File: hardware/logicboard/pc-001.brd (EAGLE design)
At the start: 25 x 61.5 mm, 15 parts, among them J4 DNP, J5 DNP

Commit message: OSHW logo.
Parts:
- added LOGO1: OSHW-LOGOL, SparkFun-Aesthetics:OSHW-LOGO-L
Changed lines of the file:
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@@
 <layer number="26" name="bNames" color="7" fill="1" visible="yes" active="yes"/>
 <layer number="27" name="tValues" color="7" fill="1" visible="yes" active="yes"/>
-<layer number="28" name="bValues" color="7" fill="1" visible="yes" active="yes"/>
+<layer number="28" name="bValues" color="7" fill="1" visible="no" active="yes"/>
 <layer number="29" name="tStop" color="7" fill="3" visible="yes" active="yes"/>
 <layer number="30" name="bStop" color="7" fill="6" visible="yes" active="yes"/>
@@
 <element name="J5" library="SparkFun-Connectors" library_urn="urn:adsk.eagle:library:513" package="1X14" package3d_urn="urn:adsk.eagle:package:38183/1" value="DNP" x="22.66" y="6.3516" smashed="yes" rot="R90">
 <attribute name="NAME" x="22.66" y="42" size="0.6096" layer="25" font="vector" ratio="20" rot="R90" align="center"/>
-<attribute name="VALUE" x="24.692" y="5.0816" size="0.6096" layer="27" font="vector" ratio="20" rot="R90"/>
+<attribute name="VALUE" x="24.692" y="5.0816" size="0.6096" layer="26" font="vector" ratio="20" rot="R90"/>
 </element>
 <element name="J4" library="SparkFun-Connectors" library_urn="urn:adsk.eagle:library:513" package="1X14" package3d_urn="urn:adsk.eagle:package:38183/1" value="DNP" x="2.34" y="39.3716" smashed="yes" rot="R270">
 <attribute name="NAME" x="2.34" y="42" size="0.6096" layer="25" font="vector" ratio="20" rot="R270" align="center"/>
-<attribute name="VALUE" x="0.308" y="40.6416" size="0.6096" layer="27" font="vector" ratio="20" rot="R270"/>
+<attribute name="VALUE" x="0.308" y="40.6416" size="0.6096" layer="26" font="vector" ratio="20" rot="R270"/>
 </element>
 <element name="RN1" library="resistor-net" library_urn="urn:adsk.eagle:library:343" package="RN-5" package3d_urn="urn:adsk.eagle:package:24976/1" value="10k" x="5.5" y="37" smashed="yes" rot="MR270">
@@
 <attribute name="VALUE" x="20.12" y="12.268" size="0.6096" layer="28" font="vector" ratio="20" rot="MR0"/>
 </element>
+<element name="LOGO1" library="SparkFun-Aesthetics" package="OSHW-LOGO-L" value="OSHW-LOGOL" x="12.5" y="53"/>
 </elements>
 <signals>

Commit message: Pineapple logo v2.
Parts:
- added U$1: PINEAPPLELOGO2, pineapplelogo2:PINEAPPLELOGO2
- LOGO1: value OSHW-LOGOL -> OSHW-LOGOS-COPPER; device SparkFun-Aesthetics:OSHW-LOGO-L -> SparkFun-Aesthetics:OSHW-LOGO-S_COPPER
- moved LOGO1 1.00 mm to (12.5, 52.0)
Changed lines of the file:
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@@
 <layers>
 <layer number="1" name="Top" color="4" fill="1" visible="yes" active="yes"/>
-<layer number="16" name="Bottom" color="1" fill="1" visible="yes" active="yes"/>
+<layer number="16" name="Bottom" color="1" fill="1" visible="no" active="yes"/>
 <layer number="17" name="Pads" color="2" fill="1" visible="yes" active="yes"/>
 <layer number="18" name="Vias" color="2" fill="1" visible="yes" active="yes"/>
@@
 <layer number="26" name="bNames" color="7" fill="1" visible="yes" active="yes"/>
 <layer number="27" name="tValues" color="7" fill="1" visible="yes" active="yes"/>
-<layer number="28" name="bValues" color="7" fill="1" visible="no" active="yes"/>
+<layer number="28" name="bValues" color="7" fill="1" visible="yes" active="yes"/>
 <layer number="29" name="tStop" color="7" fill="3" visible="yes" active="yes"/>
 <layer number="30" name="bStop" color="7" fill="6" visible="yes" active="yes"/>
@@
 <layer number="59" name="tCarbon" color="7" fill="1" visible="no" active="no"/>
 <layer number="60" name="bCarbon" color="7" fill="1" visible="no" active="no"/>
+<layer number="88" name="SimResults" color="9" fill="1" visible="no" active="no"/>
+<layer number="89" name="SimProbes" color="9" fill="1" visible="no" active="no"/>
 <layer number="90" name="Modules" color="5" fill="1" visible="no" active="no"/>
 <layer number="91" name="Nets" color="2" fill="1" visible="no" active="no"/>
@@
 <wire x1="2.3" y1="57.3" x2="0.05" y2="57.3" width="0.254" layer="42"/>
 <wire x1="4.2" y1="59.25" x2="4.2" y2="61.45" width="0.254" layer="42"/>
-<wire x1="20.8" y1="59.25" x2="20.8" y2="61.55" width="0.254" layer="42"/>
+<wire x1="20.8" y1="59.25" x2="20.8" y2="61.45" width="0.254" layer="42"/>
 <wire x1="22.7" y1="57.25" x2="24.95" y2="57.25" width="0.254" layer="42"/>
 <text x="12.5" y="58" size="1.27" layer="25" align="bottom-center">PineappleCake 1.0.0
@@
 <circle x="2.25" y="2.25" radius="1.97230625" width="0.254" layer="42"/>
 <circle x="22.75" y="2.25" radius="1.97230625" width="0.254" layer="42"/>
-<wire x1="2.3" y1="4.3" x2="0.05" y2="4.3" width="0.254" layer="42"/>
+<wire x1="2.3" y1="4.25" x2="0.05" y2="4.25" width="0.254" layer="42"/>
 <wire x1="4.2" y1="0.25" x2="4.2" y2="2.45" width="0.254" layer="42"/>
 <wire x1="20.8" y1="0.25" x2="20.8" y2="2.55" width="0.254" layer="42"/>
@@
 <attribute name="VALUE" x="20.12" y="12.268" size="0.6096" layer="28" font="vector" ratio="20" rot="MR0"/>
 </element>
-<element name="LOGO1" library="SparkFun-Aesthetics" package="OSHW-LOGO-L" value="OSHW-LOGOL" x="12.5" y="53"/>
+<element name="LOGO1" library="SparkFun-Aesthetics" package="OSHW-LOGO-S_COPPER" value="OSHW-LOGOS-COPPER" x="12.5" y="52"/>
+<element name="U$1" library="pineapplelogo2" package="PINEAPPLELOGO2" value="PINEAPPLELOGO2" x="12.5" y="54"/>
 </elements>
 <signals>
@@
 <wire x1="19.558" y1="41.91" x2="19.5" y2="42.08" width="0.254" layer="1"/>
 <via x="9.144" y="18.542" extent="1-16" drill="0.3"/>
-<polygon width="0.254" layer="1">
+<polygon width="0.127" layer="1">
 <vertex x="0" y="0"/>
 <vertex x="25" y="0"/>
-<vertex x="25" y="62"/>
-<vertex x="0" y="62"/>
+<vertex x="25" y="61"/>
+<vertex x="0" y="61"/>
 </polygon>
-<polygon width="0.254" layer="16">
+<polygon width="0.127" layer="16">
 <vertex x="0" y="0"/>
 <vertex x="25" y="0"/>
-<vertex x="25" y="62"/>
-<vertex x="0" y="62"/>
+<vertex x="25" y="61"/>
+<vertex x="0" y="61"/>
 </polygon>
 </signal>

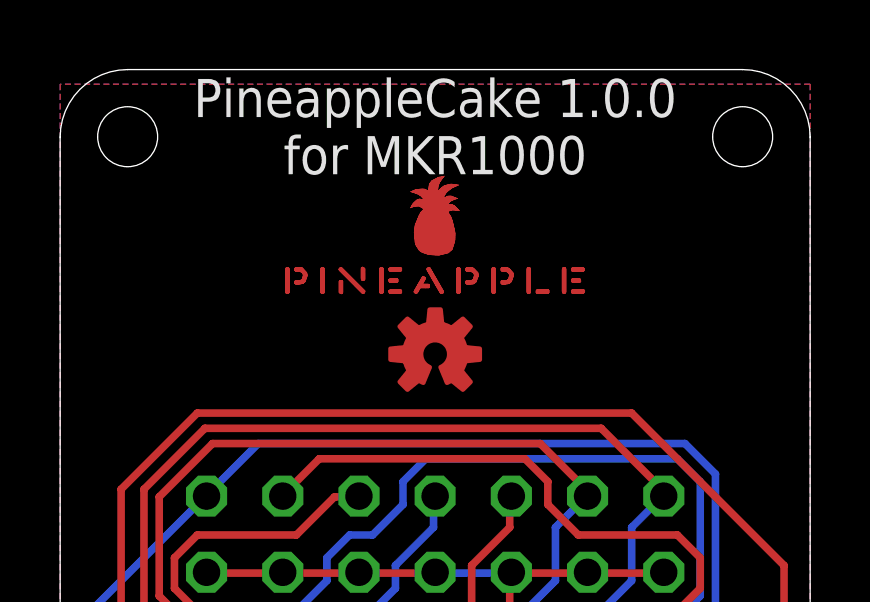
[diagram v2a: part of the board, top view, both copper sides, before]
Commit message: New pineapple logo.
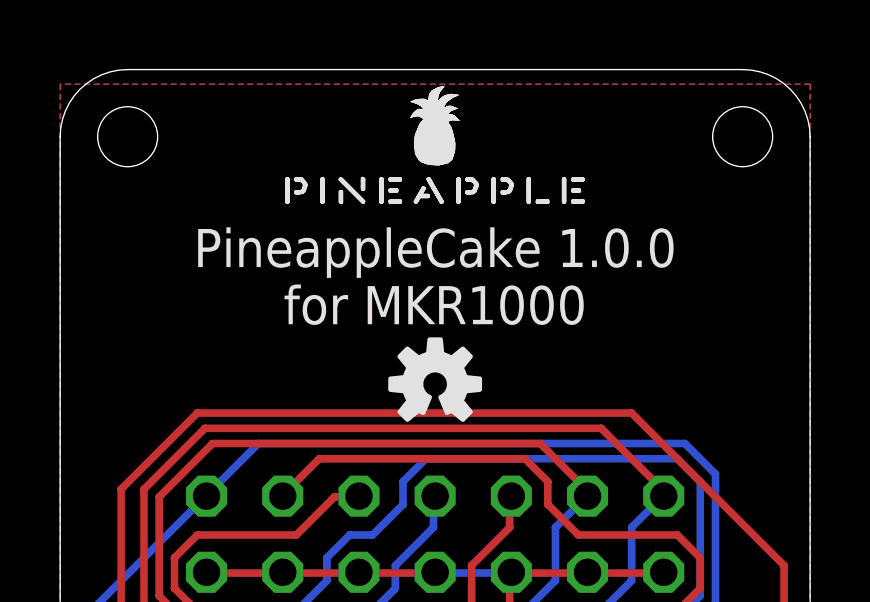
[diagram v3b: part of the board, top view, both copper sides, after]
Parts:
- removed U$1: PINEAPPLELOGO2, pineapplelogo2:PINEAPPLELOGO2
- added U$2: PINEAPPLELOGO2SILKMINI, pineapplelogo:PINEAPPLELOGO2SILKMINI
- LOGO1: value OSHW-LOGOS-COPPER -> OSHW-LOGOS; device SparkFun-Aesthetics:OSHW-LOGO-S_COPPER -> SparkFun-Aesthetics:OSHW-LOGO-S
- moved LOGO1 1.00 mm to (12.5, 51.0)
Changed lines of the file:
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@@
 <layers>
 <layer number="1" name="Top" color="4" fill="1" visible="yes" active="yes"/>
-<layer number="16" name="Bottom" color="1" fill="1" visible="no" active="yes"/>
+<layer number="16" name="Bottom" color="1" fill="1" visible="yes" active="yes"/>
 <layer number="17" name="Pads" color="2" fill="1" visible="yes" active="yes"/>
 <layer number="18" name="Vias" color="2" fill="1" visible="yes" active="yes"/>
@@
 <wire x1="20.8" y1="59.25" x2="20.8" y2="61.45" width="0.254" layer="42"/>
 <wire x1="22.7" y1="57.25" x2="24.95" y2="57.25" width="0.254" layer="42"/>
-<text x="12.5" y="58" size="1.27" layer="25" align="bottom-center">PineappleCake 1.0.0
+<text x="12.5" y="53" size="1.27" layer="25" align="bottom-center">PineappleCake 1.0.0
 for MKR1000</text>
 <hole x="17.58" y="27" drill="3.2"/>
@@
 <attribute name="VALUE" x="20.12" y="12.268" size="0.6096" layer="28" font="vector" ratio="20" rot="MR0"/>
 </element>
-<element name="LOGO1" library="SparkFun-Aesthetics" package="OSHW-LOGO-S_COPPER" value="OSHW-LOGOS-COPPER" x="12.5" y="52"/>
-<element name="U$1" library="pineapplelogo2" package="PINEAPPLELOGO2" value="PINEAPPLELOGO2" x="12.5" y="54"/>
+<element name="LOGO1" library="SparkFun-Aesthetics" package="OSHW-LOGO-S" value="OSHW-LOGOS" x="12.5" y="51"/>
+<element name="U$2" library="pineapplelogo" package="PINEAPPLELOGO2SILKMINI" value="PINEAPPLELOGO2SILKMINI" x="12.5" y="57"/>
 </elements>
 <signals>

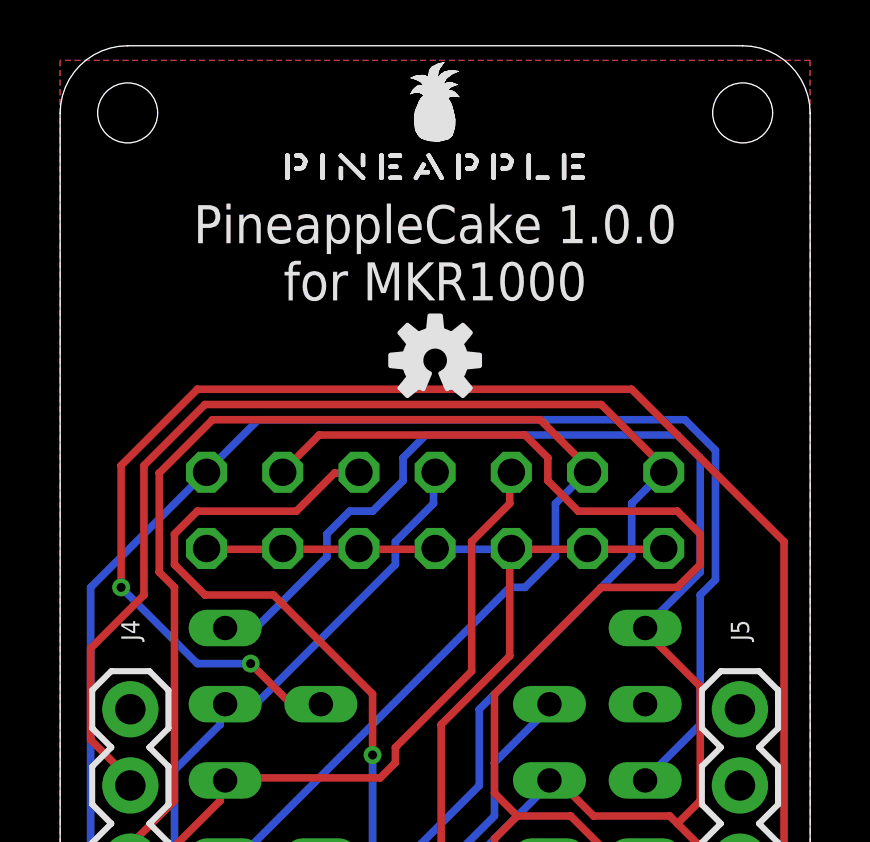
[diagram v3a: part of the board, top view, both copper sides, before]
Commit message: Updated silk pattern.
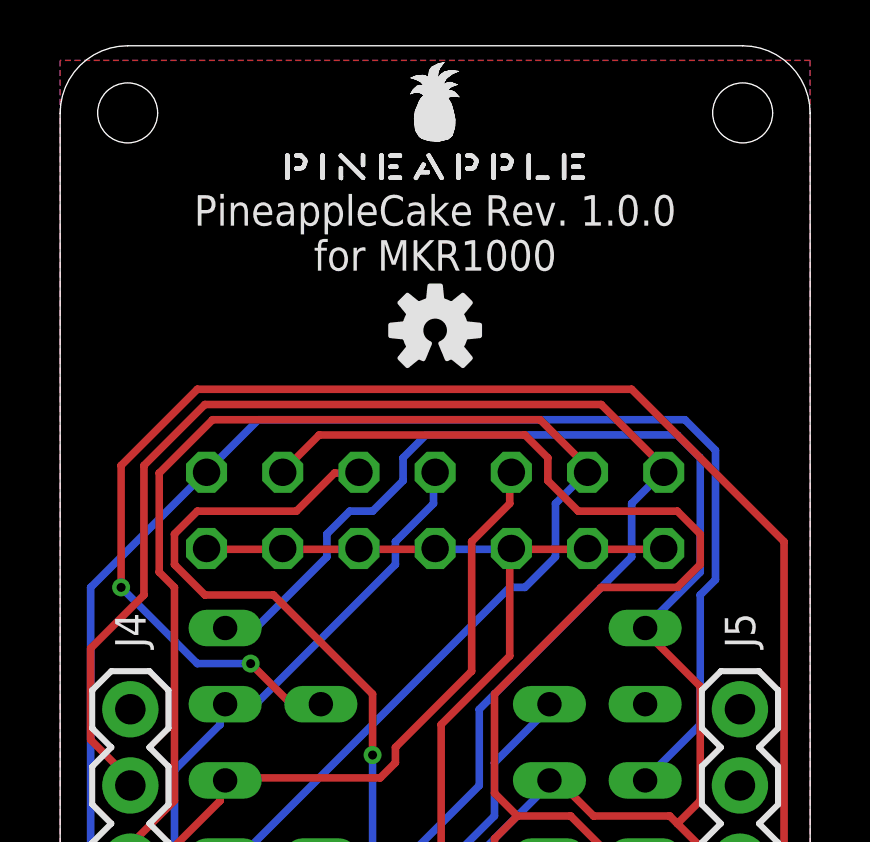
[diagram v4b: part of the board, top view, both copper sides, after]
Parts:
- moved LOGO1 1.00 mm to (12.5, 52.0)
- renumbered LED1 to L1, LED2 to L2
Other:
- board text added: "PineappleCake Rev. 1.0.0"
- board text added: "for MKR1000"
- board text removed: "PineappleCake 1.0.0 for MKR1000"

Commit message: Changed signal names.
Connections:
- net LED1K renamed D4
- net LED2K renamed D5
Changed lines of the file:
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@@
 <wire x1="4.826" y1="47.244" x2="4.88" y2="47.27" width="0.254" layer="16"/>
 </signal>
-<signal name="LED1K">
+<signal name="D4">
 <contactref element="J4" pad="13"/>
 <contactref element="L1" pad="2"/>
@@
 <wire x1="2.54" y1="8.89" x2="2.34" y2="8.8916" width="0.254" layer="16"/>
 </signal>
-<signal name="LED2K">
+<signal name="D5">
 <contactref element="L2" pad="2"/>
 <contactref element="J4" pad="14"/>

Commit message: Version number 1.0.0 -> 2.0.0.
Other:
- board text added: "PineappleCake Rev. 2.0.0"
- board text removed: "PineappleCake Rev. 1.0.0"
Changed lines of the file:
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@@
 <wire x1="20.8" y1="59.25" x2="20.8" y2="61.45" width="0.254" layer="42"/>
 <wire x1="22.7" y1="57.25" x2="24.95" y2="57.25" width="0.254" layer="42"/>
-<text x="12.5" y="56" size="1.016" layer="25" align="center">PineappleCake Rev. 1.0.0</text>
+<text x="12.5" y="56" size="1.016" layer="25" align="center">PineappleCake Rev. 2.0.0</text>
 <hole x="17.58" y="27" drill="3.2"/>
 <hole x="7.42" y="27" drill="3.2"/>
